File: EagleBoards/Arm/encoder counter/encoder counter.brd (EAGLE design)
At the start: 160 x 100 mm, 15 parts, among them X2 22-23-2021_100MILHEADER, X3 22-23-2041, X4 22-23-2021_100MILHEADER, X5 22-23-2021_100MILHEADER, X6 22-23-2021_100MILHEADER

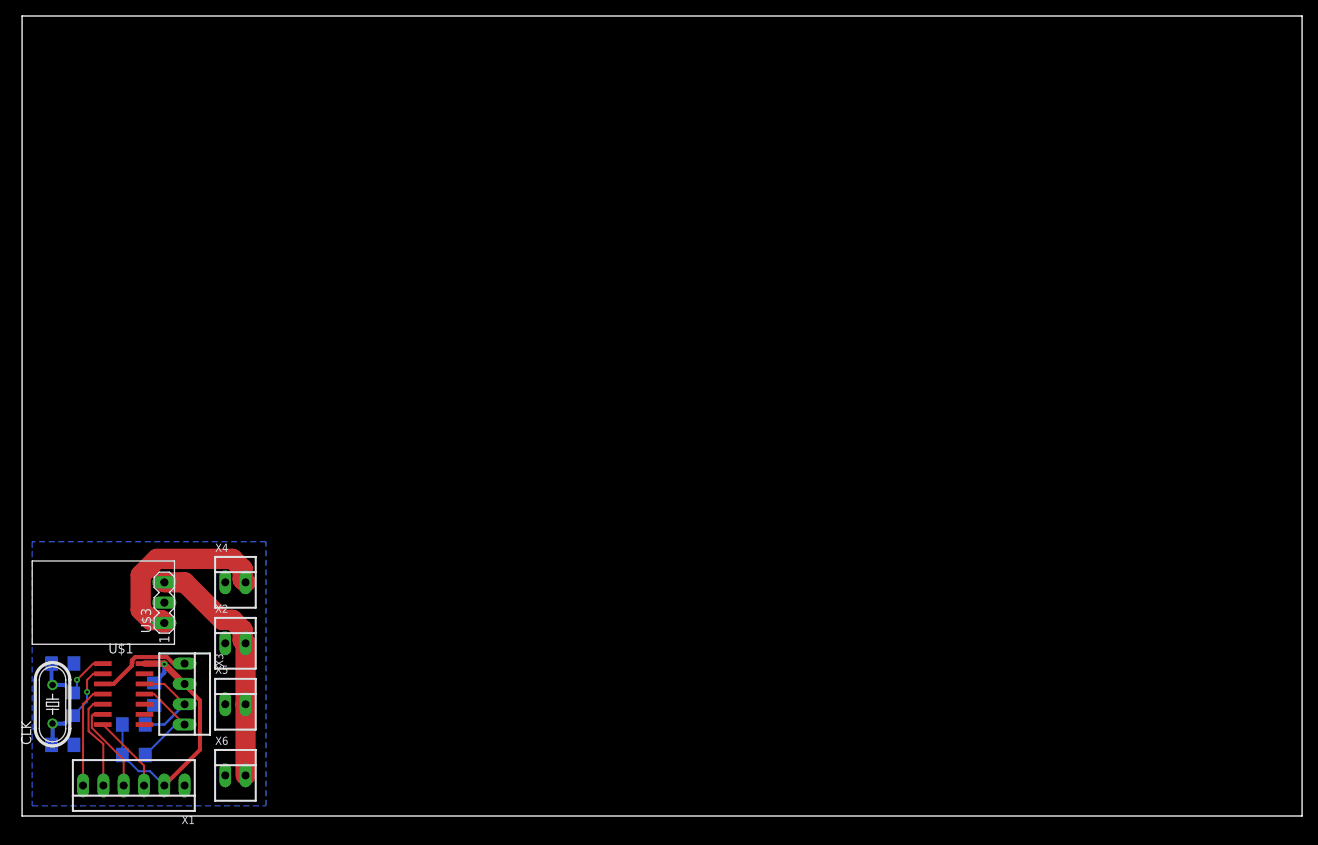
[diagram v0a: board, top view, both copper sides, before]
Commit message: encoder boards done
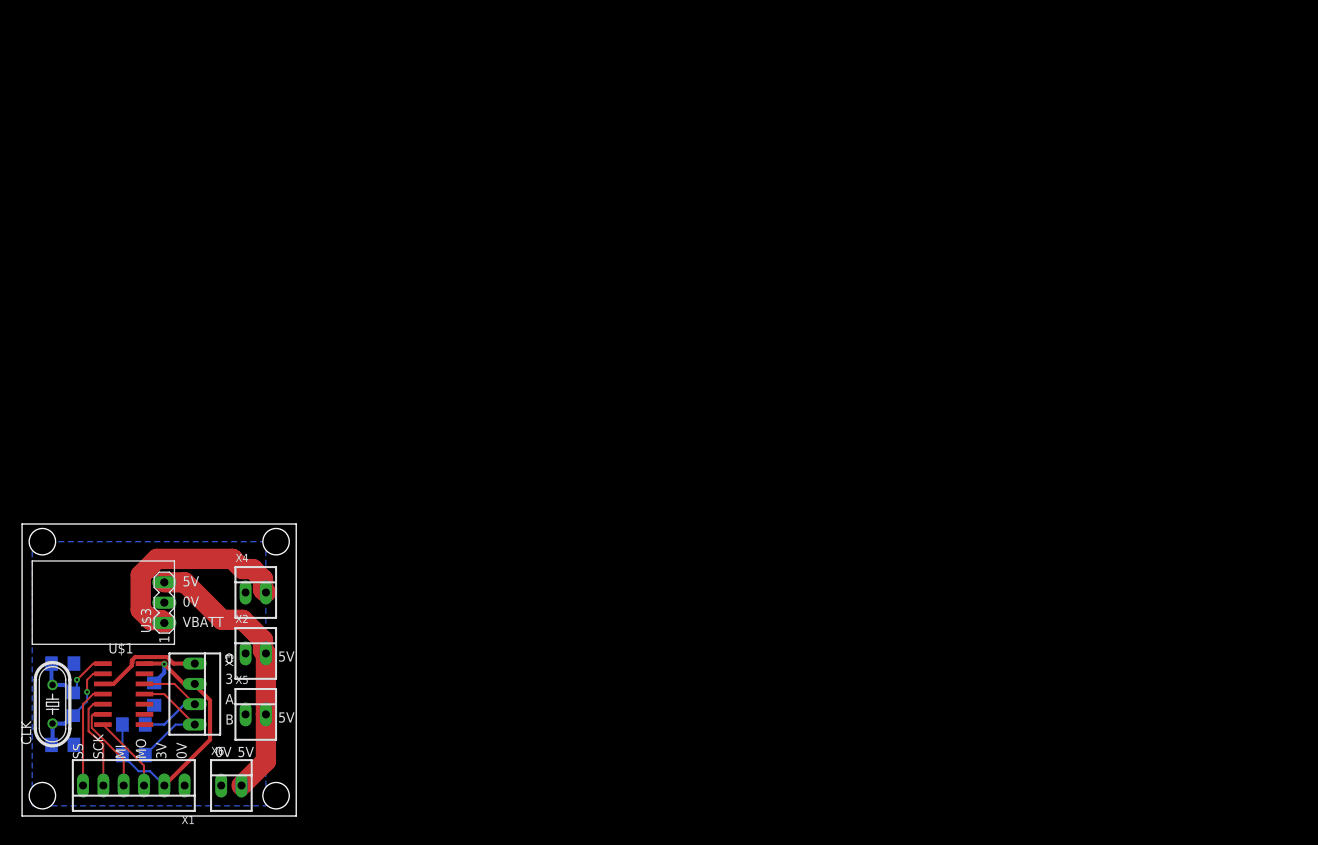
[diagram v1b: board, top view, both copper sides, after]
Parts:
- moved X5 2.84 mm to (29.2, 12.7)
- moved X2 2.84 mm to (29.2, 20.3)
- moved X4 2.84 mm to (29.2, 27.9)
- moved X6 1.37 mm to (26.2, 3.81)
- moved X3 1.27 mm to (21.6, 15.2)
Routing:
- net VCC5: track 30.6 -> 34.9 mm
- net VIN: track 23.9 -> 27.0 mm
- net B: track 13.1 -> 15.6 mm
- net A: track 12.1 -> 14.6 mm
- net VCC3: track 35.0 -> 36.7 mm
- net GND: track 12.7 -> 14.0 mm
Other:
- board size 160 x 100 mm -> 34.3 x 36.5 mm
- board text added: "0"
- board text added: "0V"
- board text added: "3"
- board text added: "3V"
- board text added: "5V"
- board text added: "A"
- board text added: "B"
- board text added: "MI"
- board text added: "MO"
- board text added: "SCK"
- board text added: "SS"
- board text added: "VBATT"

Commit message: printed designs with gerbers
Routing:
- net VIN: track 27.0 -> 15.4 mm
- net VCC5: track 34.9 -> 33.1 mm
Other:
- outline, holes or cut-outs redrawn
- board text added: "Husky Robotics Team 2018"
- board text added: "Quadrature Decoder"
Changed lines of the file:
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@@
 <board>
 <plain>
-<wire x1="0" y1="0" x2="34.27" y2="0" width="0" layer="20"/>
-<wire x1="34.27" y1="0" x2="34.27" y2="36.5" width="0" layer="20"/>
-<wire x1="34.27" y1="36.5" x2="0" y2="36.5" width="0" layer="20"/>
-<wire x1="0" y1="36.5" x2="0" y2="0" width="0" layer="20"/>
+<wire x1="0" y1="34.5" x2="0" y2="2" width="0" layer="20"/>
+<wire x1="0" y1="2" x2="2" y2="0" width="0" layer="20" curve="90"/>
+<wire x1="2" y1="0" x2="32.27" y2="0" width="0" layer="20"/>
+<wire x1="32.27" y1="0" x2="34.27" y2="2" width="0" layer="20" curve="90"/>
+<wire x1="34.27" y1="2" x2="34.27" y2="34.5" width="0" layer="20"/>
+<wire x1="34.27" y1="34.5" x2="32.27" y2="36.5" width="0" layer="20" curve="90"/>
+<wire x1="32.27" y1="36.5" x2="2" y2="36.5" width="0" layer="20"/>
+<wire x1="2" y1="36.5" x2="0" y2="34.5" width="0" layer="20" curve="90"/>
 <hole x="2.54" y="34.29" drill="3.302"/>
 <hole x="31.75" y="34.29" drill="3.302"/>
@@
 <text x="25.4" y="13.97" size="1.27" layer="21">A</text>
 <text x="25.4" y="11.43" size="1.27" layer="21">B</text>
-<text x="20.066" y="28.702" size="1.27" layer="21">5V</text>
+<text x="20.066" y="23.622" size="1.27" layer="21">5V</text>
 <text x="20.066" y="26.162" size="1.27" layer="21">0V</text>
-<text x="20.066" y="23.622" size="1.27" layer="21">VBATT</text>
+<text x="20.066" y="28.702" size="1.27" layer="21">VBATT</text>
 <text x="32.004" y="11.684" size="1.27" layer="21">5V</text>
 <text x="32.004" y="19.304" size="1.27" layer="21">5V</text>
 <text x="26.924" y="7.366" size="1.27" layer="21">5V</text>
+<text x="5.08" y="34.29" size="1.4224" layer="21">Husky Robotics Team 2018</text>
+<text x="5.08" y="32.512" size="1.4224" layer="21">Quadrature Decoder</text>
 </plain>
 <attributes>
@@
 <contactref element="U$3" pad="1"/>
 <contactref element="X4" pad="2"/>
-<wire x1="14.8336" y1="25.7651875" x2="16.1131875" y2="24.4856" width="2.54" layer="1"/>
-<wire x1="16.1131875" y1="24.4856" x2="17.4244" y2="24.4856" width="2.54" layer="1"/>
-<wire x1="17.4244" y1="24.4856" x2="17.78" y2="24.13" width="2.54" layer="1"/>
-<wire x1="14.8336" y1="30.1148125" x2="14.8336" y2="25.7651875" width="2.54" layer="1"/>
-<wire x1="26.3015" y1="32.1404" x2="16.8591875" y2="32.1404" width="2.54" layer="1"/>
-<wire x1="16.8591875" y1="32.1404" x2="14.8336" y2="30.1148125" width="2.54" layer="1"/>
-<wire x1="26.3015" y1="32.1185" x2="26.3015" y2="32.1404" width="2.54" layer="1"/>
-<wire x1="26.3015" y1="32.1185" x2="27.5496" y2="30.8704" width="2.54" layer="1"/>
 <wire x1="27.5496" y1="30.8704" x2="27.5496" y2="30.8704" width="2.54" layer="1"/>
 <wire x1="27.5496" y1="30.8704" x2="28.8415" y2="30.8704" width="2.54" layer="1"/>
@@
 <wire x1="30.1164" y1="29.5955" x2="30.1164" y2="28.3036" width="2.54" layer="1"/>
 <wire x1="30.1164" y1="28.3036" x2="30.48" y2="27.94" width="2.54" layer="1"/>
+<wire x1="27.5496" y1="30.8704" x2="19.4404" y2="30.8704" width="2.54" layer="1"/>
+<wire x1="19.4404" y1="30.8704" x2="17.78" y2="29.21" width="2.54" layer="1"/>
 </signal>
 <signal name="VCC5">
@@
 <contactref element="X6" pad="2"/>
 <contactref element="X5" pad="2"/>
-<wire x1="17.78" y1="29.21" x2="20.32" y2="29.21" width="2.54" layer="1"/>
-<wire x1="25.0096" y1="24.5204" x2="20.32" y2="29.21" width="2.54" layer="1"/>
 <wire x1="30.48" y1="12.7" x2="30.48" y2="20.32" width="2.54" layer="1"/>
 <wire x1="30.48" y1="20.32" x2="30.1164" y2="20.6836" width="2.54" layer="1"/>
 <wire x1="30.1164" y1="20.6836" x2="30.1164" y2="21.9755" width="2.54" layer="1"/>
 <wire x1="30.1164" y1="21.9755" x2="27.5715" y2="24.5204" width="2.54" layer="1"/>
-<wire x1="27.5715" y1="24.5204" x2="25.0096" y2="24.5204" width="2.54" layer="1"/>
 <wire x1="27.432" y1="3.81" x2="30.48" y2="6.858" width="2.54" layer="1"/>
 <wire x1="30.48" y1="6.858" x2="30.48" y2="12.7" width="2.54" layer="1"/>
+<wire x1="19.4816125" y1="24.5204" x2="19.4468125" y2="24.4856" width="2.54" layer="1"/>
+<wire x1="19.4468125" y1="24.4856" x2="18.1356" y2="24.4856" width="2.54" layer="1"/>
+<wire x1="18.1356" y1="24.4856" x2="17.78" y2="24.13" width="2.54" layer="1"/>
+<wire x1="27.5715" y1="24.5204" x2="19.4816125" y2="24.5204" width="2.54" layer="1"/>
 </signal>
 <signal name="SS">
